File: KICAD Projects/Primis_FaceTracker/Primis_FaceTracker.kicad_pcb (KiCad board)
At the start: 2 copper layers, 47 parts, among them CN2 KH-FG0.5-H2.0-24PIN, J1 USB_C_Receptacle_USB2.0_16P, Q1 PMOS, SW1 SW_SPST, SW2 SW_SPST, U1 ESP32-S3-WROOM-1, U2 AMS1117-3.3, U3 XC6206P122MR, U5 XC6206P282MR

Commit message: Face Tracker PCB
-Some work on the PCB, not quite done but I'm making some changes so uploading as a backup.
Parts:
- moved H3 92.9 mm to (120.6, 129.3)
- moved H2 71.7 mm to (120.6, 79.3)
- moved C1 62.6 mm to (128.2, 91.5), turned to -90 degrees
- moved C8 59.2 mm to (132.3, 103.0)
- moved H4 57.6 mm to (204.6, 129.3)
- moved C9 55.2 mm to (138.0, 110.5), turned to 90 degrees
- moved C4 54.4 mm to (135.2, 89.8)
- moved C10 52.9 mm to (138.0, 105.8), turned to 90 degrees
- moved D4 52.1 mm to (142.8, 97.7), turned to 90 degrees
- moved D1 51.1 mm to (142.8, 76.8), turned to 90 degrees
- moved R10 45.6 mm to (118.1, 92.2)
- moved R2 44.7 mm to (140.2, 76.7), turned to -90 degrees
- moved SW2 42.7 mm to (180.4, 92.4)
- moved R6 42.1 mm to (198.4, 85.6), turned to 90 degrees
- moved R1 41.3 mm to (118.1, 89.0), turned to 180 degrees
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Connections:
- net Net-(U1-USB_D+) renamed D+
- net Net-(U1-USB_D-) renamed D-
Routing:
- net CAM_RST: track 0.00 -> 141.7 mm, vias 0 -> 2
- net +5V: track 0.00 -> 71.7 mm, vias 0 -> 4
- net D+: track 0.00 -> 61.5 mm, vias 0 -> 2
- net D-: track 0.00 -> 61.3 mm, vias 0 -> 2
- net GND: track 0.00 -> 55.9 mm, vias 0 -> 32
- net Net-(Q1-D): track 0.00 -> 39.2 mm, vias 0 -> 2
- net CAM_MCLK: track 0.00 -> 36.0 mm, vias 0 -> 2
- net CAM_1.2V: track 0.00 -> 34.7 mm, vias 0 -> 2
- net CAM_SDA: track 0.00 -> 33.7 mm
- net CAM_SCK: track 0.00 -> 32.9 mm
- net CAM_2.8V: track 0.00 -> 28.9 mm
- net CAM_PCLK: track 0.00 -> 22.4 mm
- net CAM_VSYNC: track 0.00 -> 20.3 mm
- net CAM_D7: track 0.00 -> 20.3 mm
- net CAM_HSYNC: track 0.00 -> 20.2 mm
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
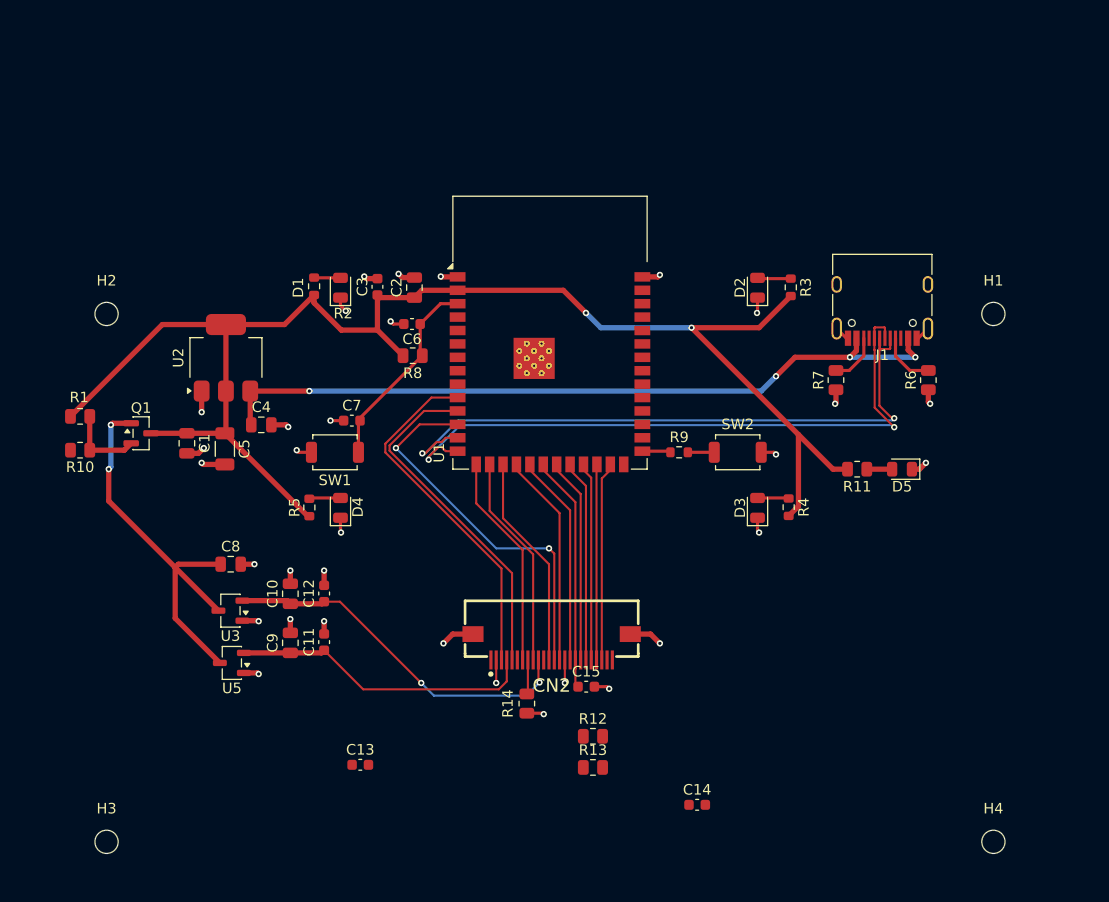
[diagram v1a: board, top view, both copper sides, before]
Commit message: Face Tracker V1
-Roughly finished face tracker PCB
-Organised face tracker schematics
-Added face tracker images
-Added USB-C and FPC port models
-Updated README
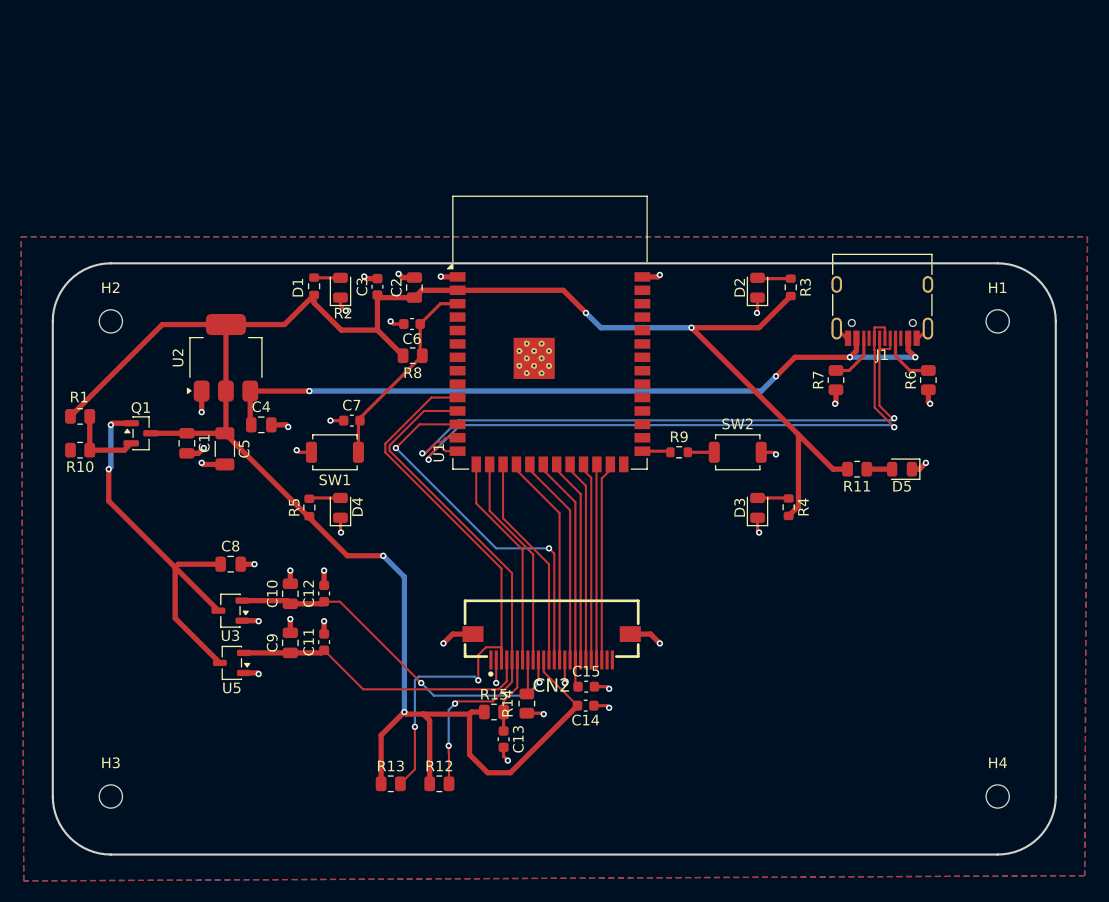
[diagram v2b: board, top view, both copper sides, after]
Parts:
- added R15: 4.7k, Resistor_SMD:R_0805_2012Metric, F.Cu at (157.3, 117.0)
- moved R13 19.2 mm to (147.5, 123.8)
- moved R12 15.2 mm to (152.1, 123.8)
- moved C14 14.1 mm to (166.0, 116.4)
- moved C13 13.8 mm to (158.2, 119.6), turned to -90 degrees
- moved H3 4.31 mm to (121.0, 125.0)
- moved H4 4.31 mm to (205.0, 125.0)
- moved H1 0.81 mm to (205.0, 80.0)
- moved H2 0.81 mm to (121.0, 80.0)
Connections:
- C1 pad 1: CAM_RST -> +3V3
- C14 pad 1: CAM_RST -> +3V3
- C2 pad 1: CAM_RST -> +3V3
- C3 pad 1: CAM_RST -> +3V3
- C5 pad 1: CAM_RST -> +3V3
- CN2 pad 11: CAM_RST -> +3V3
- Q1 pad 3: CAM_RST -> +3V3
- R1 pad 2: CAM_RST -> +3V3
- R11 pad 2: CAM_RST -> +3V3
- R12 pad 1: CAM_RST -> +3V3
- R13 pad 1: CAM_RST -> +3V3
- R2 pad 2: CAM_RST -> +3V3
- R3 pad 2: CAM_RST -> +3V3
- R4 pad 2: CAM_RST -> +3V3
- R5 pad 2: CAM_RST -> +3V3
- R8 pad 2: CAM_RST -> +3V3
- U1 pad 2: CAM_RST -> +3V3
- U2 pad 2: CAM_RST -> +3V3
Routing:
- net +3V3: track 0.00 -> 211.3 mm, vias 0 -> 4
- net CAM_RST: track 141.7 -> 7.27 mm, vias 2 -> 0
- net CAM_SDA: track 33.7 -> 56.4 mm, vias 0 -> 2
- net CAM_SCK: track 32.9 -> 49.1 mm, vias 0 -> 2
- net GND: track 55.9 -> 58.9 mm, vias 32 -> 34
- added copper zone on B.Cu, net GND
- added copper zone on F.Cu, net GND
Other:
- board outline added: 95 x 56 mm
